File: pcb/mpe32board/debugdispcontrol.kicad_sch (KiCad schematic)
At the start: 16 parts, among them SW3 SW_Push, SW4 SW_Push, SW5 SW_Push, SW6 SW_Push

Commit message: create lcd footprint
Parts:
- SW3, SW4, SW5, SW6: footprint Button_Switch_Keyboard:SW_Cherry_MX_1.00u_PCB -> mxfoot:MX-Hotswap-1U
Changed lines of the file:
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@@
 			)
 		)
-		(property "Footprint" "Button_Switch_Keyboard:SW_Cherry_MX_1.00u_PCB"
+		(property "Footprint" "mxfoot:MX-Hotswap-1U"
 			(at 157.48 60.96 0)
 			(effects
@@
 			)
 		)
-		(property "Footprint" "Button_Switch_Keyboard:SW_Cherry_MX_1.00u_PCB"
+		(property "Footprint" "mxfoot:MX-Hotswap-1U"
 			(at 119.38 60.96 0)
 			(effects
@@
 			)
 		)
-		(property "Footprint" "Button_Switch_Keyboard:SW_Cherry_MX_1.00u_PCB"
+		(property "Footprint" "mxfoot:MX-Hotswap-1U"
 			(at 78.74 60.96 0)
 			(effects
@@
 			)
 		)
-		(property "Footprint" "Button_Switch_Keyboard:SW_Cherry_MX_1.00u_PCB"
+		(property "Footprint" "mxfoot:MX-Hotswap-1U"
 			(at 198.12 60.96 0)
 			(effects

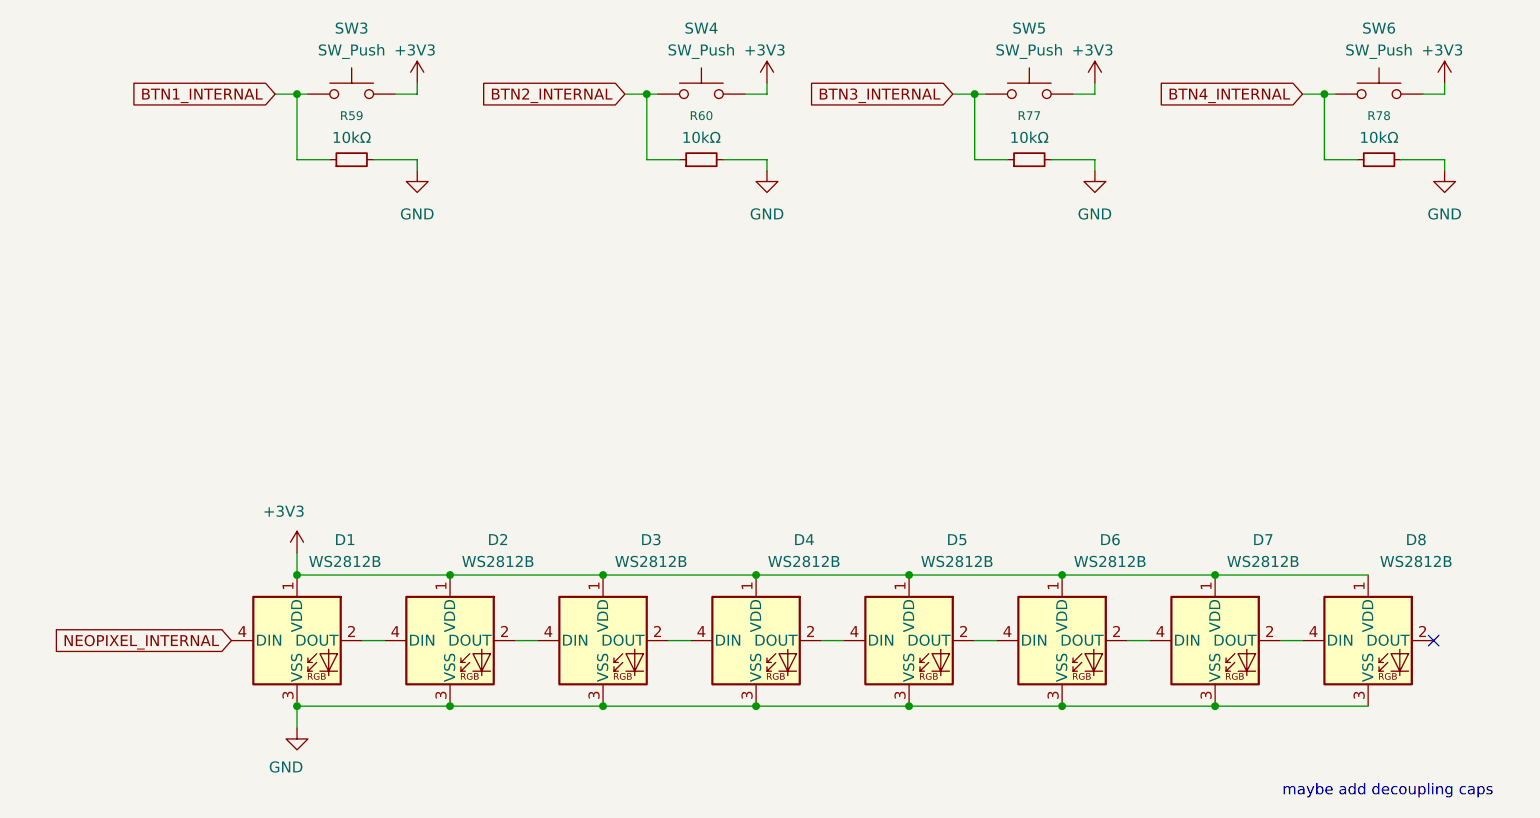
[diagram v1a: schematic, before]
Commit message: routed data bus of ram
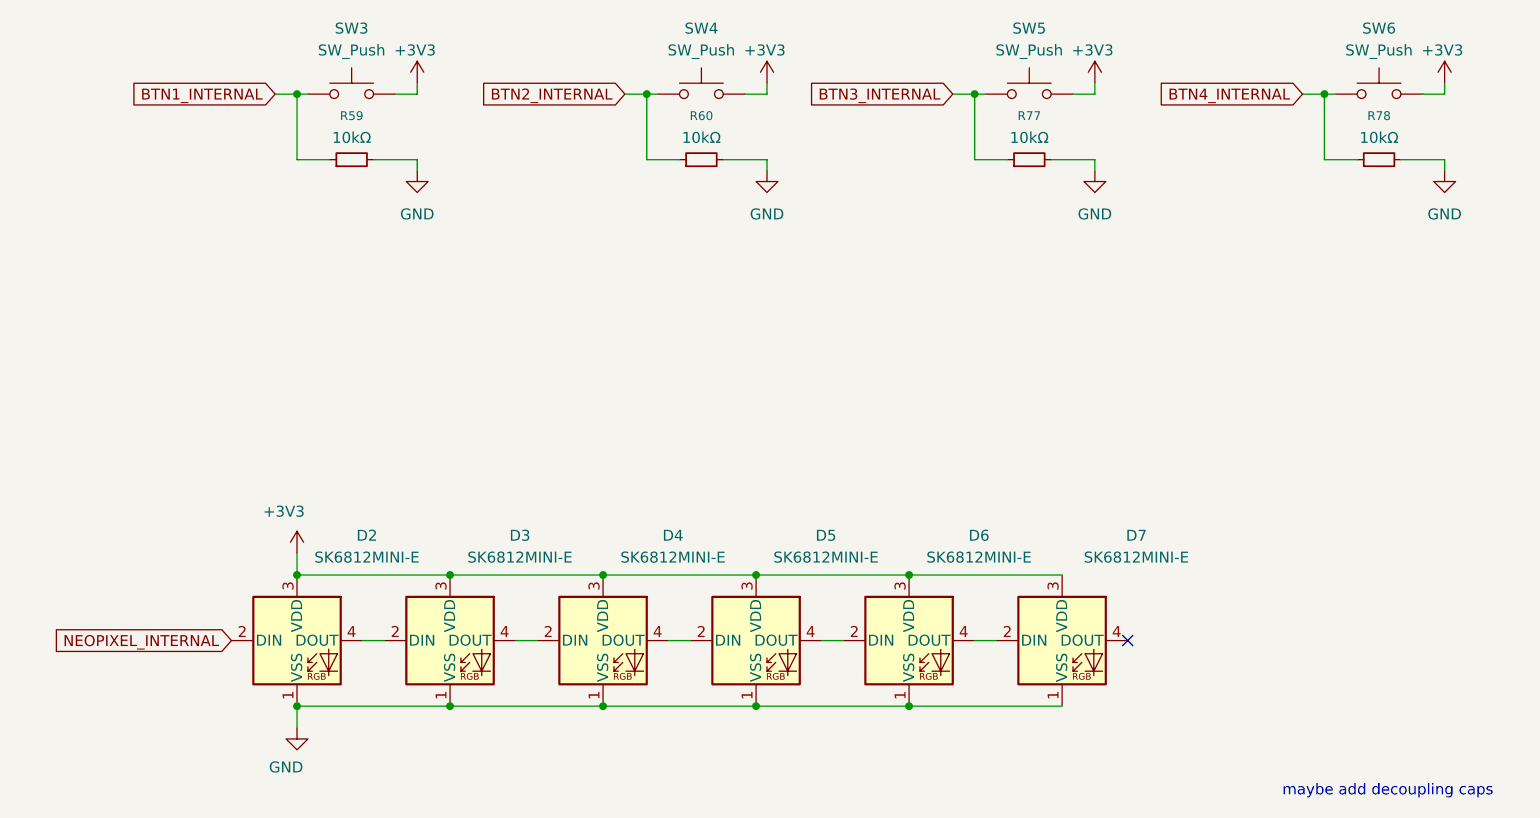
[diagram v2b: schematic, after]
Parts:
- removed D1, D2, D3, D4, D5, D6, D7, D8: WS2812B, LED_SMD:LED_WS2812B_PLCC4_5.0x5.0mm_P3.2mm, symbol LED:WS2812B
- added D2, D3, D4, D5, D6, D7: SK6812MINI-E, LED_SMD:LED_SK6812MINI-E_3.2x2.8mm_P1.5mm_ReverseMount, symbol LED:SK6812MINI-E
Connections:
- net +3V3: now also D2.3 (VDD), D3.3 (VDD), D4.3 (VDD), D5.3 (VDD), D6.3 (VDD), D7.3 (VDD)
- net GND: now also D2.1 (VSS), D3.1 (VSS), D4.1 (VSS), D5.1 (VSS), D6.1 (VSS), D7.1 (VSS)
- net NEOPIXEL_INTERNAL: now also D2.2 (DIN)
- new net: D3.4 (DOUT), D4.2 (DIN)
- new net: D4.4 (DOUT), D5.2 (DIN)
- new net: D5.4 (DOUT), D6.2 (DIN)
- new net: D6.4 (DOUT), D7.2 (DIN)
- new net: D2.4 (DOUT), D3.2 (DIN)
